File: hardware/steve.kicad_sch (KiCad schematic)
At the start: 34 parts, among them J1 Conn_ARM_JTAG_SWD_10, J5 USB_C_Receptacle_16P, SW1 SW_SPST, SW2 SW_SPST, U1 STM32F407VGTx, U3 TLV1117LV33DCYR, U6 W25Q128JVSIQ, Y1 12MHz, Y2 32.768kHz

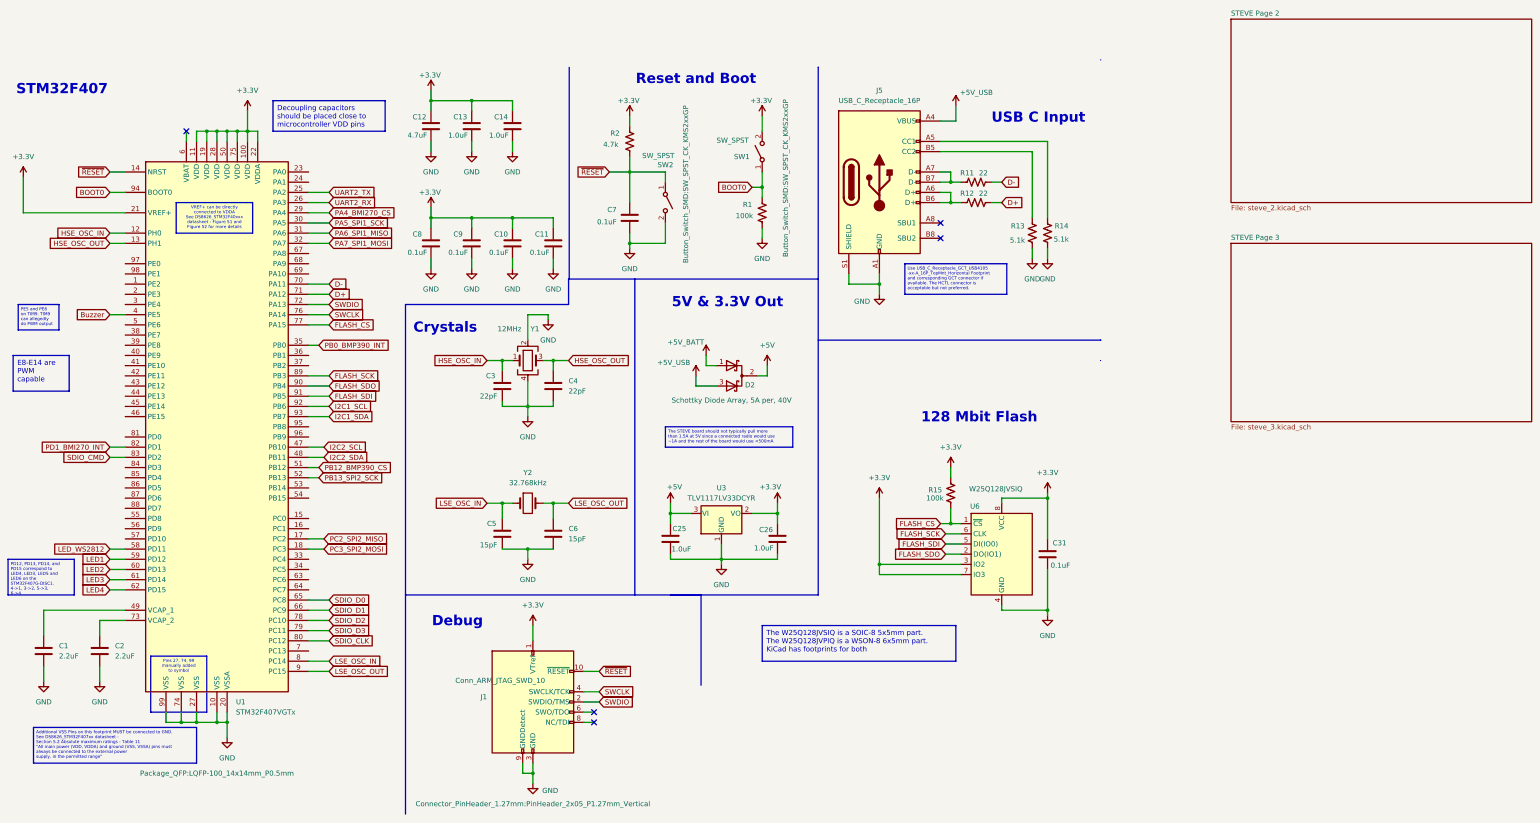
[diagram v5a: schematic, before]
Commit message: Finished schematic
Finished schematic - 3D model fixes using custom imports, all important parts sourced, additional GPIO/bus pins broken out, PSM board signals broken out, battery voltage sense line added.
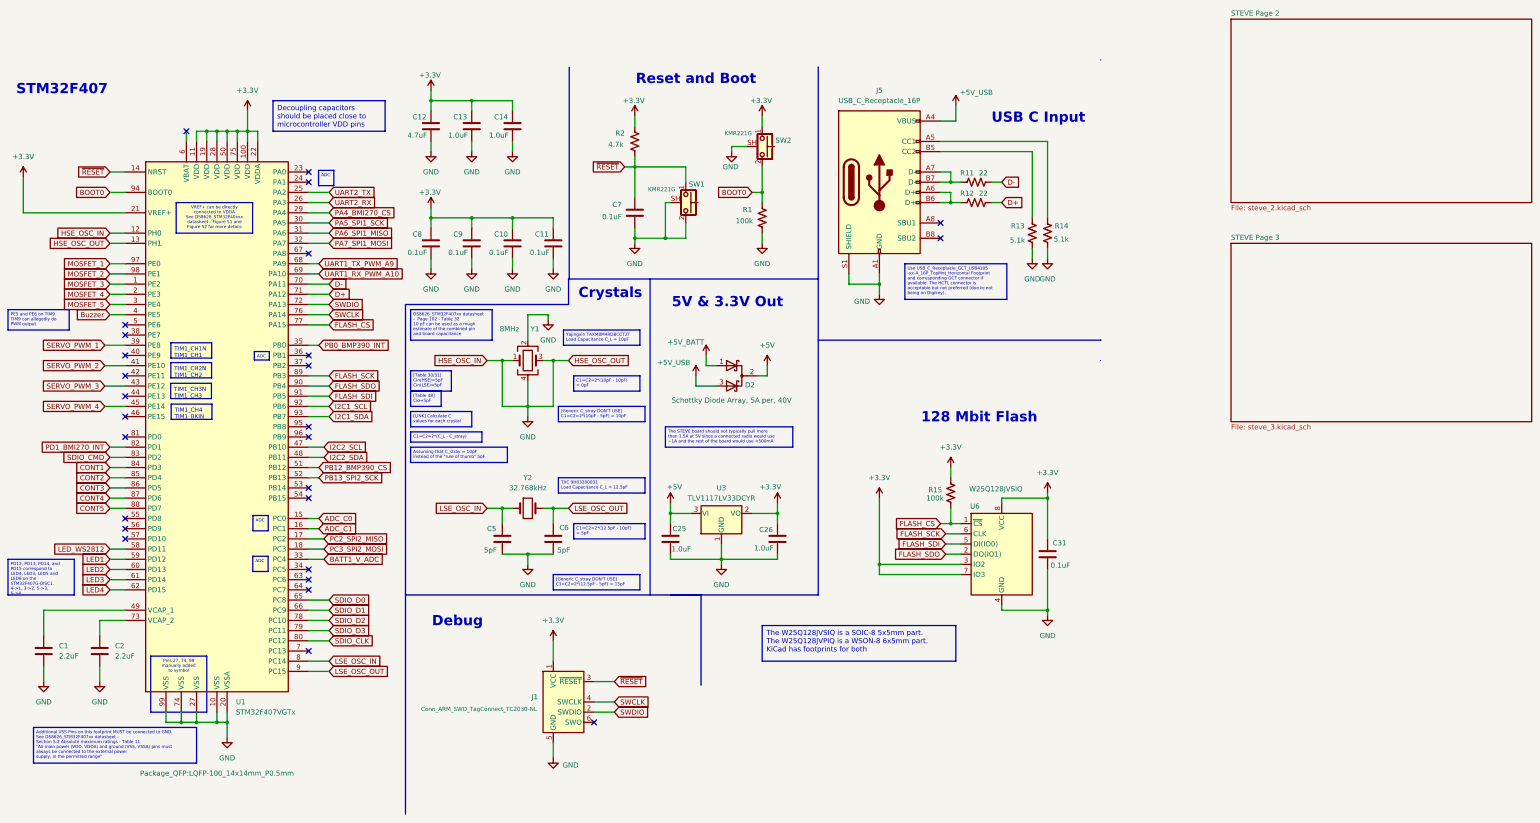
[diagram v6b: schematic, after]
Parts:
- removed C3, C4: 22pF, Capacitor_SMD:C_0603_1608Metric, symbol Device:C
- removed J1: Conn_ARM_JTAG_SWD_10, Connector_PinHeader_1.27mm:PinHeader_2x05_P1.27mm_Vertical, symbol Connector:Conn_ARM_JTAG_SWD_10
- removed SW1, SW2: SW_SPST, Button_Switch_SMD:SW_SPST_CK_KMS2xxGP, symbol Switch:SW_SPST
- added J1: Conn_ARM_SWD_TagConnect_TC2030-NL, Connector:Tag-Connect_TC2030-IDC-NL_2x03_P1.27mm_Vertical, symbol Connector:Conn_ARM_SWD_TagConnect_TC2030-NL
- added SW1, SW2: KMR221G, Imported_Footprints:SW_Push_3D_1P1T-SH_NO_CK_KMR2xxG, symbol Switch:CK_KMS2xxG
- C5, C6: value 15pF -> 5pF
- J5: footprint Connector_USB:USB_C_Receptacle_HCTL_HC-TYPE-C-16P-01A -> Imported_Footprints:USB_C_Receptacle_3D_HCTL_HC-TYPE-C-16P-01A
- U6: footprint Package_SO:SOIC-8_5.23x5.23mm_P1.27mm -> Imported_Footprints:SOIC-8_5.23x5.23mm_P1.27mm_3D
- Y1: value 12MHz -> 8MHz
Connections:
- net HSE_OSC_IN is gone; now on net GND: U1.12 (PH0), Y1.1
- net HSE_OSC_OUT is gone; now on net GND: U1.13 (PH1), Y1.3
- net +3.3V: now also J1.1 (VCC), SW2.1
- net BOOT0: now also SW2.2
- net GND: now also J1.5 (GND), SW1.2, SW1.SH (B), SW2.SH (B)
- net SWCLK: now also J1.4 (SWCLK)
- net SWDIO: now also J1.2 (SWDIO)
- net ~{RESET}: now also J1.3 (~{RESET}), SW1.1
- net MOSFET_3: now reaches U1.1 (PE2)
- net ADC_C0: now reaches U1.15 (PC0)
- net ADC_C1: now reaches U1.16 (PC1)
- net MOSFET_4: now reaches U1.2 (PE3)
- net MOSFET_5: now reaches U1.3 (PE4)
- net BATT1_V_ADC: now reaches U1.33 (PC4)
- net SERVO_PWM_1: now reaches U1.39 (PE8)
- net SERVO_PWM_2: now reaches U1.41 (PE10)
- net SERVO_PWM_3: now reaches U1.43 (PE12)
- net SERVO_PWM_4: now reaches U1.45 (PE14)
- net UART1_TX_PWM_A9: now reaches U1.68 (PA9)
- net UART1_RX_PWM_A10: now reaches U1.69 (PA10)
- net CONT1: now reaches U1.84 (PD3)
- net CONT2: now reaches U1.85 (PD4)
- net CONT3: now reaches U1.86 (PD5)
- net CONT4: now reaches U1.87 (PD6)
- net CONT5: now reaches U1.88 (PD7)
- net MOSFET_1: now reaches U1.97 (PE0)
- net MOSFET_2: now reaches U1.98 (PE1)
- no-connect marks 5 -> 27
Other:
- moved on the sheet: C5, C6, C7, R1, R2, Y2

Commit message: started component layout
started component layout - attempting to use a 60x60mm board size
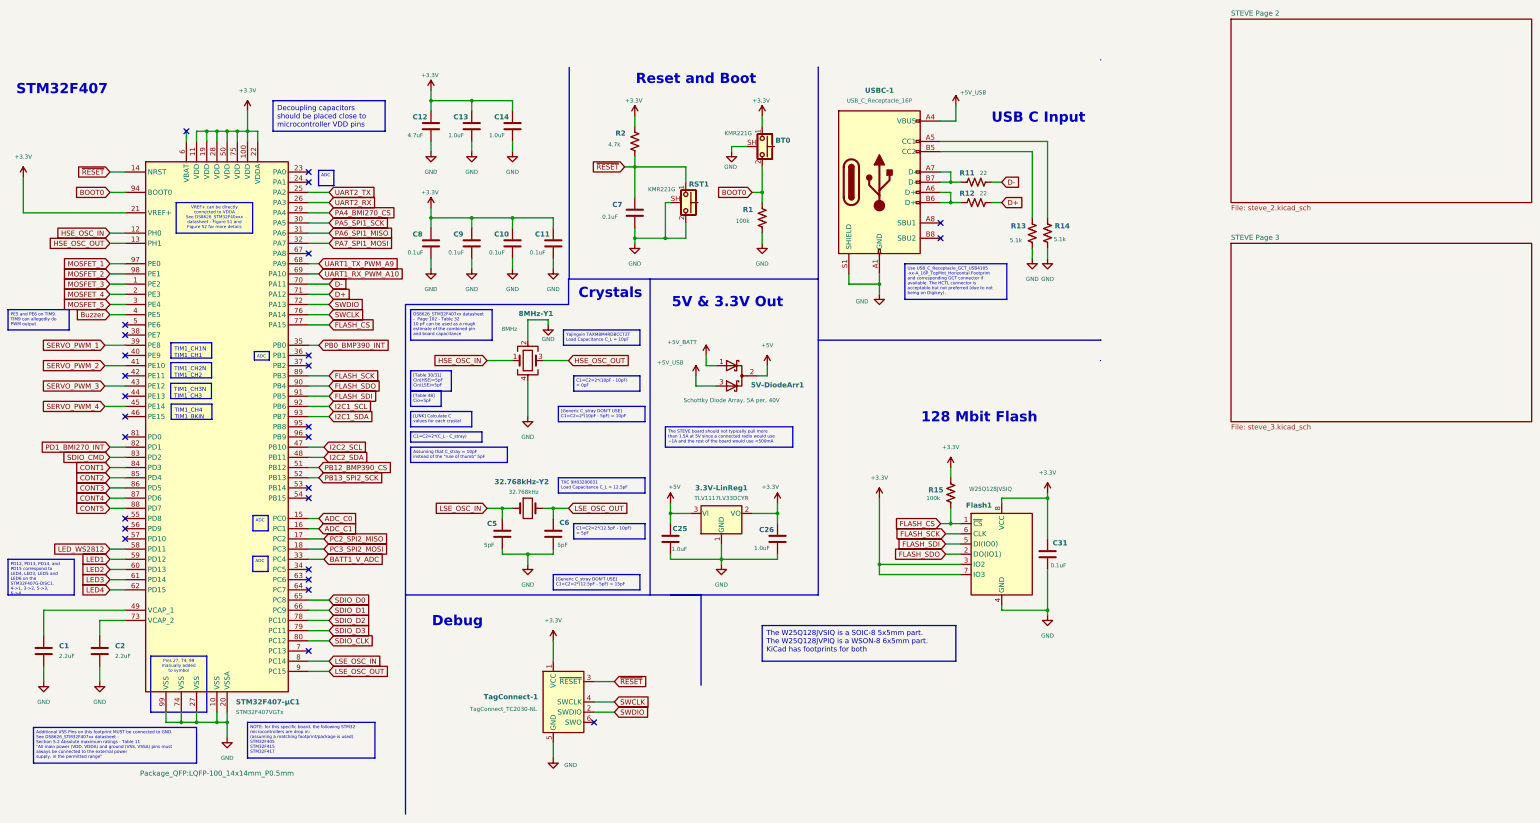
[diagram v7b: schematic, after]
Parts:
- TagConnect-1: renamed from J1; value Conn_ARM_SWD_TagConnect_TC2030-NL -> TagConnect_TC2030-NL
- renumbered U3 to 3.3V-LinReg1, Y2 to 32.768kHz-Y2, D2 to 5V-DiodeArr1, Y1 to 8MHz-Y1, SW2 to BT0, U6 to Flash1, SW1 to RST1, U1 to STM32F407-µC1, J5 to USBC-1
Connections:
- net GND: no longer 8MHz-Y1.1, 8MHz-Y1.3, STM32F407-µC1.12 (PH0), STM32F407-µC1.13 (PH1)
- new net HSE_OSC_IN: 8MHz-Y1.1, STM32F407-µC1.12 (PH0)
- new net HSE_OSC_OUT: 8MHz-Y1.3, STM32F407-µC1.13 (PH1)
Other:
- moved on the sheet: C5, C6
